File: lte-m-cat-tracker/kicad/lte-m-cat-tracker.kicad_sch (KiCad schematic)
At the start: 35 parts, among them J1 JST-PH-2mm-2P, J2 USB-C-16P, SW1 MSK12C02, U1 SIM7080G-M, U2 ESP32-C3, U3 LIS2DW12TR, U4 TP4056, U5 XC6220B331MR-G

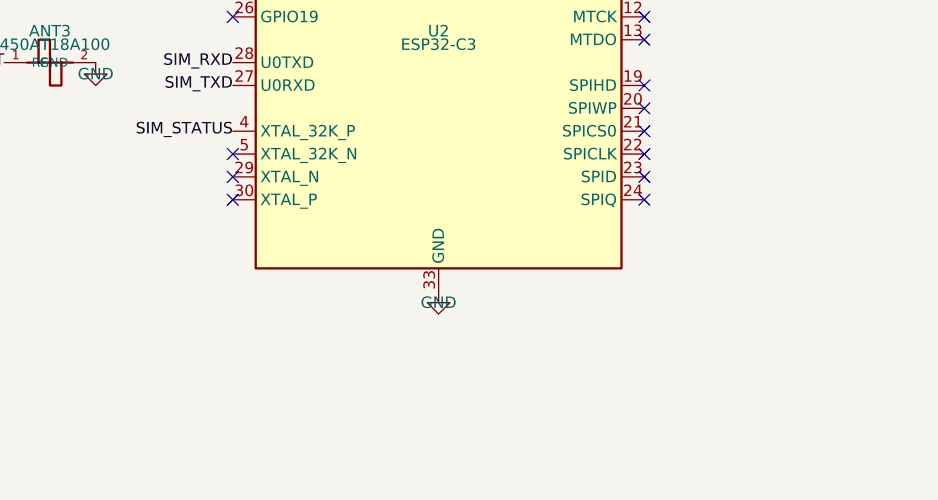
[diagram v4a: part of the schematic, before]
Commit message: 回路図に水晶Y1(C648974)+C16/C17を反映・schematic-parity解消（ネットリスト検証でPCBと一致確認・ERC水晶起因エラーなし）
Co-Authored-By: Claude Fable 5 <noreply@anthropic.com>
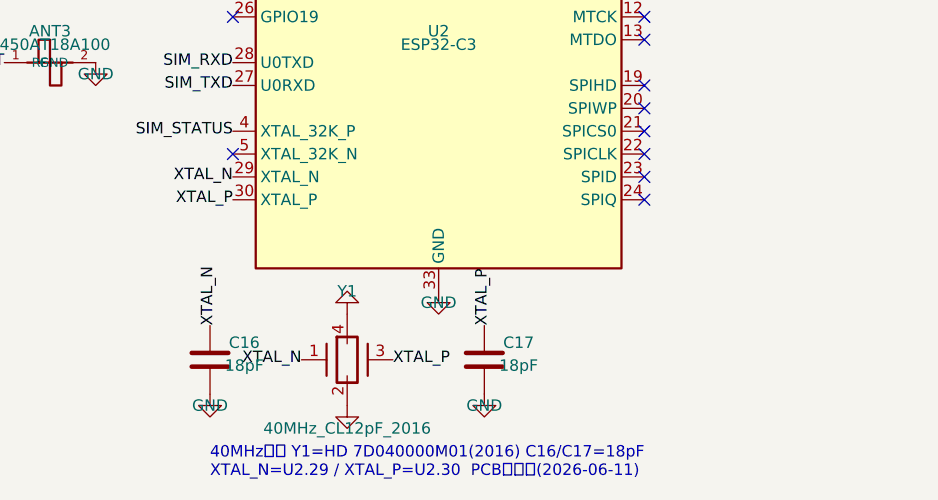
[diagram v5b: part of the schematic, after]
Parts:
- added C16, C17: 18pF, Capacitor_SMD:C_0402_1005Metric, symbol Device:C
- added Y1: 40MHz_CL12pF_2016, Crystal:Crystal_SMD_2016-4Pin_2.0x1.6mm, symbol Device:Crystal_GND24
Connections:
- net GND: now also C16.2, C17.2, Y1.2, Y1.4
- net XTAL_N: now reaches U2.29 (XTAL_N)
- net XTAL_N: now also C16.1, Y1.1
- net XTAL_P: now reaches U2.30 (XTAL_P)
- net XTAL_P: now also C17.1, Y1.3
- no-connect marks 27 -> 25
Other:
- note added: "40MHz水晶 Y1=HD 7D040000M01(2016) C16/C17=18pF XTAL_N=U2.29 / XTAL_P=U2.30 PCB実装済(2026-06-11)"
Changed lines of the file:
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@@
   (no_connect (at 111.76 215.9))
   (no_connect (at 66.04 210.82))
-  (no_connect (at 66.04 213.36))
-  (no_connect (at 66.04 215.9))
   (symbol (lib_id "Device:C") (at 63.49999999999999 165.1 0) (unit 1)
     (exclude_from_sim no)(in_bom yes)(on_board yes)
@@
     (property "Value" "GND"(at 93.98 81.28 0)(effects(font(size 1.27 1.27))))
     (property "Footprint" ""(at 93.98 80.01 0)(effects(font(size 1.27 1.27))hide)))
-)
+  (label "XTAL_N" (at 66.04 213.36 180)
+    (effects(font(size 1.27 1.27))(justify right))
+)
+  (label "XTAL_P" (at 66.04 215.9 180)
+    (effects(font(size 1.27 1.27))(justify right))
+)
+  (symbol (lib_id "Device:Crystal_GND24") (at 78.74 233.68 0) (unit 1)
+    (exclude_from_sim no)(in_bom yes)(on_board yes)
+    (property "Reference" "Y1" (at 78.74 226.06 0)(effects(font(size 1.27 1.27))))
+    (property "Value" "40MHz_CL12pF_2016" (at 78.74 241.3 0)(effects(font(size 1.27 1.27))))
+    (property "Footprint" "Crystal:Crystal_SMD_2016-4Pin_2.0x1.6mm" (at 78.74 233.68 0)(effects(font(size 1.27 1.27))hide))
+    (property "LCSC" "C648974" (at 78.74 233.68 0)(effects(font(size 1.27 1.27))hide))
+  )
+  (label "XTAL_N" (at 73.66 233.68 180)
+    (effects(font(size 1.27 1.27))(justify right))
+)
+  (label "XTAL_P" (at 83.82 233.68 0)
+    (effects(font(size 1.27 1.27))(justify left))
+)
+  (symbol (lib_id "power:GND") (at 78.74 238.76 0)(unit 1)
+    (exclude_from_sim no)(in_bom no)(on_board no)
+    (property "Reference" "#PWR"(at 78.74 241.3 0)(effects(font(size 1.27 1.27))hide))
+    (property "Value" "GND"(at 78.74 240.03 0)(effects(font(size 1.27 1.27))hide))
+    (property "Footprint" ""(at 78.74 238.76 0)(effects(font(size 1.27 1.27))hide)))
+  (symbol (lib_id "power:GND") (at 78.74 228.6 180)(unit 1)
+    (exclude_from_sim no)(in_bom no)(on_board no)
+    (property "Reference" "#PWR"(at 78.74 226.06 0)(effects(font(size 1.27 1.27))hide))
+    (property "Value" "GND"(at 78.74 227.33 0)(effects(font(size 1.27 1.27))hide))
+    (property "Footprint" ""(at 78.74 228.6 0)(effects(font(size 1.27 1.27))hide)))
+  (symbol (lib_id "Device:C") (at 63.5 233.68 0) (unit 1)
+    (exclude_from_sim no)(in_bom yes)(on_board yes)
+    (property "Reference" "C16" (at 67.31 231.775 0)(effects(font(size 1.27 1.27))))
+    (property "Value" "18pF" (at 67.31 234.315 0)(effects(font(size 1.27 1.27))))
+    (property "Footprint" "Capacitor_SMD:C_0402_1005Metric" (at 63.5 233.68 0)(effects(font(size 1.27 1.27))hide))
+    (property "LCSC" "C1555(発注前要確認)" (at 63.5 233.68 0)(effects(font(size 1.27 1.27))hide))
+  )
+  (label "XTAL_N" (at 63.5 229.87 270)
+    (effects(font(size 1.27 1.27))(justify left))
+)
+  (symbol (lib_id "power:GND") (at 63.5 237.49 0)(unit 1)
+    (exclude_from_sim no)(in_bom no)(on_board no)
+    (property "Reference" "#PWR"(at 63.5 240.03 0)(effects(font(size 1.27 1.27))hide))
+    (property "Value" "GND"(at 63.5 238.76 0)(effects(font(size 1.27 1.27))))
+    (property "Footprint" ""(at 63.5 237.49 0)(effects(font(size 1.27 1.27))hide)))
+  (symbol (lib_id "Device:C") (at 93.98 233.68 0) (unit 1)
+    (exclude_from_sim no)(in_bom yes)(on_board yes)
+    (property "Reference" "C17" (at 97.79 231.775 0)(effects(font(size 1.27 1.27))))
+    (property "Value" "18pF" (at 97.79 234.315 0)(effects(font(size 1.27 1.27))))
+    (property "Footprint" "Capacitor_SMD:C_0402_1005Metric" (at 93.98 233.68 0)(effects(font(size 1.27 1.27))hide))
+    (property "LCSC" "C1555(発注前要確認)" (at 93.98 233.68 0)(effects(font(size 1.27 1.27))hide))
+  )
+  (label "XTAL_P" (at 93.98 229.87 270)
+    (effects(font(size 1.27 1.27))(justify left))
+)
+  (symbol (lib_id "power:GND") (at 93.98 237.49 0)(unit 1)
+    (exclude_from_sim no)(in_bom no)(on_board no)
+    (property "Reference" "#PWR"(at 93.98 240.03 0)(effects(font(size 1.27 1.27))hide))
+    (property "Value" "GND"(at 93.98 238.76 0)(effects(font(size 1.27 1.27))))
+    (property "Footprint" ""(at 93.98 237.49 0)(effects(font(size 1.27 1.27))hide)))
+  (text "40MHz水晶 Y1=HD 7D040000M01(2016) C16/C17=18pF\nXTAL_N=U2.29 / XTAL_P=U2.30  PCB実装済(2026-06-11)"
+    (at 63.5 245.11 0)(effects(font(size 1.27 1.27))(justify left)))
+)

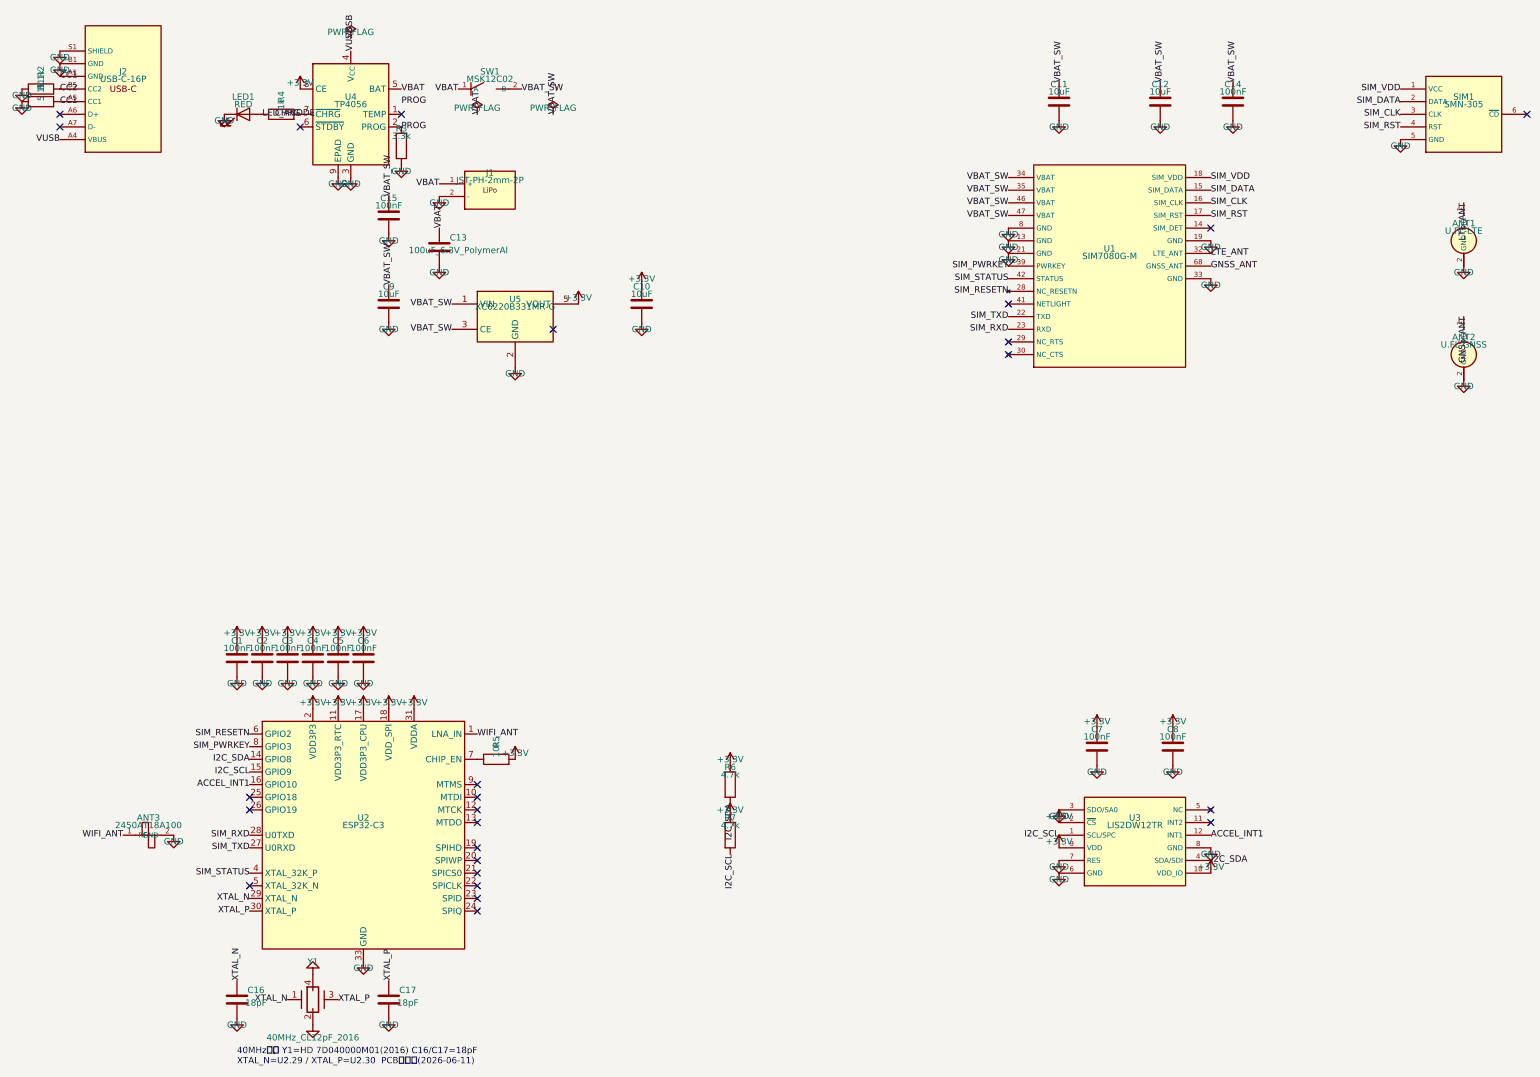
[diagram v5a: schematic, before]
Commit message: 回路図同期完了: UART1ピン修正・VDD_EXT/U6/C18/C19追加・netlist検証でPCBと一致
- U1シンボル TXD/RXD 22/23→1/2・pin46/47 NC化・VDD_EXTピン40新設
- SIM_RESETN消滅・U2側_33ネット化・U6(TXB0104)シンボル+パスコン2個
- フットプリント実体化(TXB0104_RGY14/C_0402)・ERC24件(増分は許容クラス)

Co-Authored-By: Claude Fable 5 <noreply@anthropic.com>
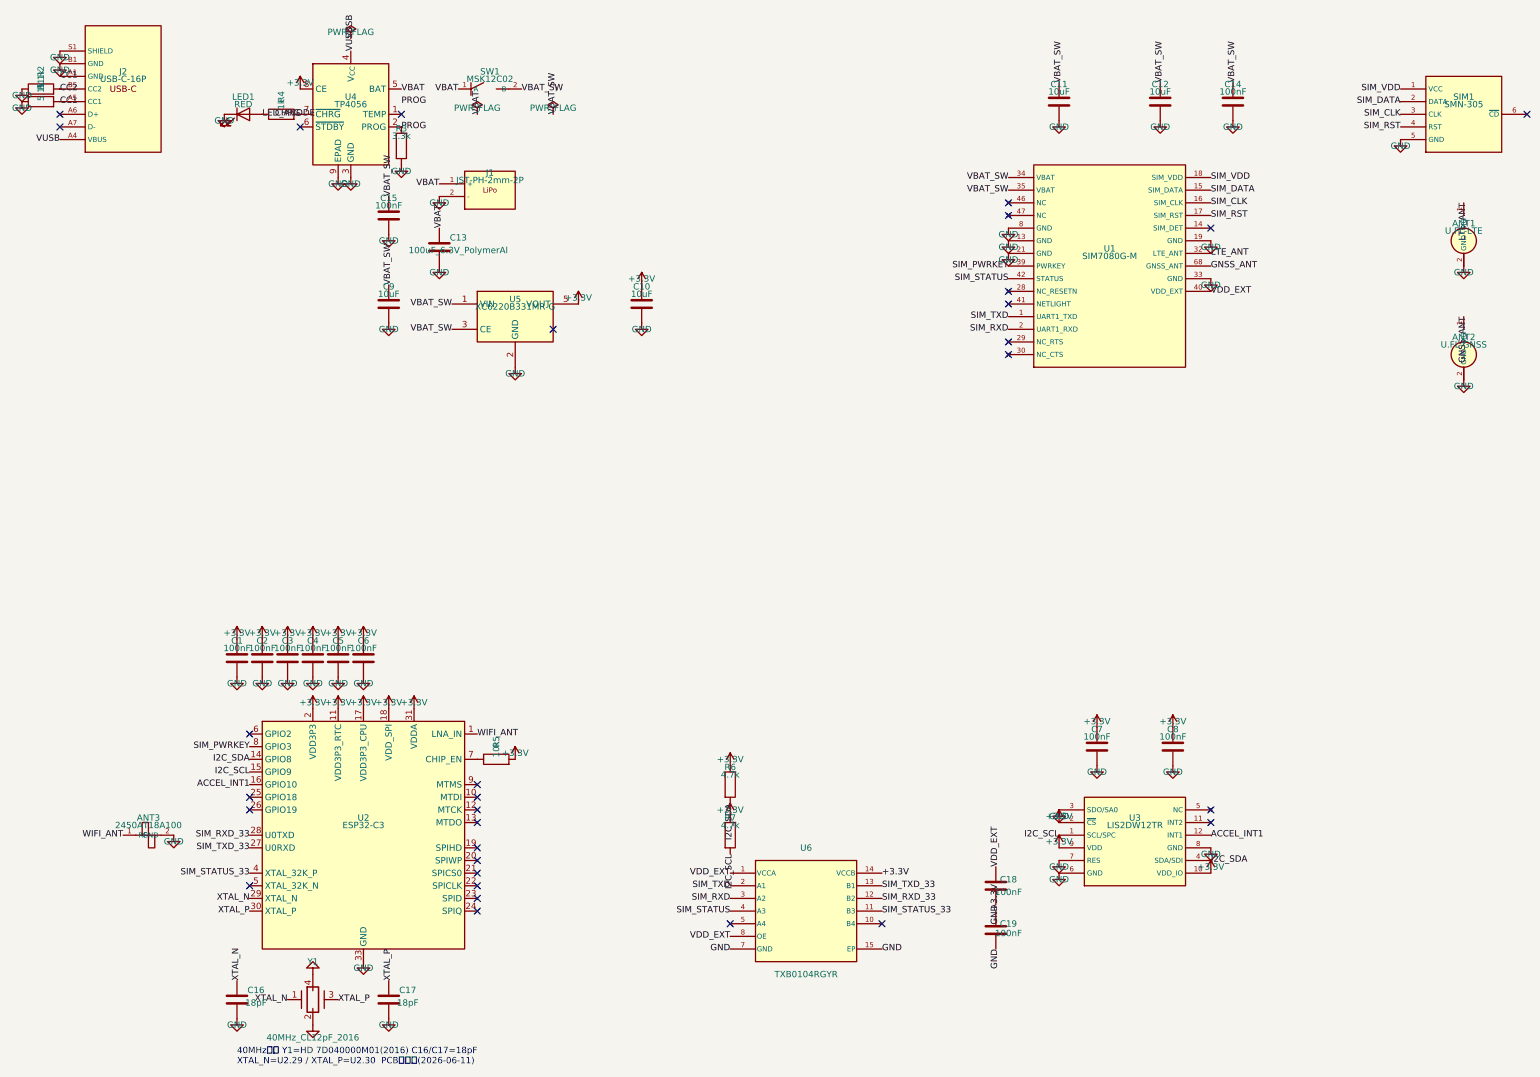
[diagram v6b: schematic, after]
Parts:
- added C18, C19: 100nF, lte-m-custom:C_0402, symbol Device:C
- added U6: TXB0104RGYR, lte-m-custom:TXB0104_RGY14, symbol Custom:TXB0104
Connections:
- net +3.3V: now also C19.1, U6.14 (VCCB)
- net GND: now also C18.2, C19.2, U6.15 (EP), U6.7 (GND)
- net SIM_RXD: now also U1.2 (UART1_RXD), U6.3 (A2); no longer U1.23 (RXD), U2.28 (U0TXD)
- net SIM_STATUS: now also U6.4 (A3); no longer U2.4 (XTAL_32K_P)
- net SIM_TXD: now also U1.1 (UART1_TXD), U6.2 (A1); no longer U1.22 (TXD), U2.27 (U0RXD)
- net VBAT_SW: no longer U1.46 (VBAT), U1.47 (VBAT)
- net SIM_RESETN: no longer names the net of U1.28 (NC_RESETN)
- net SIM_RESETN: no longer U2.6 (GPIO2)
- new net SIM_RXD_33: U2.28 (U0TXD), U6.12 (B2)
- new net SIM_STATUS_33: U2.4 (XTAL_32K_P), U6.11 (B3)
- new net SIM_TXD_33: U2.27 (U0RXD), U6.13 (B1)
- new net VDD_EXT: C18.1, U1.40 (VDD_EXT), U6.1 (VCCA), U6.8 (OE)
- no-connect marks 25 -> 31
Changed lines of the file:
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@@
     (effects(font(size 1.27 1.27))(justify right))
 )
-  (label "VBAT_SW" (at 218.44 73.66 180)
-    (effects(font(size 1.27 1.27))(justify right))
-)
-  (label "VBAT_SW" (at 218.44 76.2 180)
-    (effects(font(size 1.27 1.27))(justify right))
-)
+  (no_connect (at 218.44 73.66))
+  (no_connect (at 218.44 76.2))
   (symbol (lib_id "power:GND") (at 218.44 78.74 0)(unit 1)
     (exclude_from_sim no)(in_bom no)(on_board no)
@@
     (effects(font(size 1.27 1.27))(justify right))
 )
-  (label "SIM_RESETN" (at 218.44 91.44 180)
-    (effects(font(size 1.27 1.27))(justify right))
-)
+  (no_connect (at 218.44 91.44))
   (no_connect (at 218.44 93.98))
   (label "SIM_TXD" (at 218.44 96.52 180)
@@
   (no_connect (at 218.44 101.6))
   (no_connect (at 218.44 104.14))
+  (label "VDD_EXT" (at 259.08 91.44 0)
+    (effects(font(size 1.27 1.27))(justify left))
+)
   (label "SIM_VDD" (at 259.08 68.58 0)
     (effects(font(size 1.27 1.27))(justify left))
@@
     (effects(font(size 1.27 1.27))(justify left))
 )
-  (label "SIM_TXD" (at 66.04 203.2 180)
-    (effects(font(size 1.27 1.27))(justify right))
-)
-  (label "SIM_RXD" (at 66.04 200.66 180)
+  (label "SIM_TXD_33" (at 66.04 203.2 180)
+    (effects(font(size 1.27 1.27))(justify right))
+)
+  (label "SIM_RXD_33" (at 66.04 200.66 180)
     (effects(font(size 1.27 1.27))(justify right))
 )
@@
     (effects(font(size 1.27 1.27))(justify right))
 )
-  (label "SIM_RESETN" (at 66.04 180.34 180)
-    (effects(font(size 1.27 1.27))(justify right))
-)
-  (label "SIM_STATUS" (at 66.04 208.28 180)
+  (no_connect (at 66.04 180.34))
+  (label "SIM_STATUS_33" (at 66.04 208.28 180)
     (effects(font(size 1.27 1.27))(justify right))
 )
@@
   (text "40MHz水晶 Y1=HD 7D040000M01(2016) C16/C17=18pF\nXTAL_N=U2.29 / XTAL_P=U2.30  PCB実装済(2026-06-11)"
     (at 63.5 245.11 0)(effects(font(size 1.27 1.27))(justify left)))
-)
+  (symbol (lib_id "Custom:TXB0104") (at 177.8 215.9 0) (unit 1)
+    (exclude_from_sim no)(in_bom yes)(on_board yes)
+    (property "Reference" "U6" (at 177.8 203.20000000000002 0)(effects(font(size 1.27 1.27))))
+    (property "Value" "TXB0104RGYR" (at 177.8 228.6 0)(effects(font(size 1.27 1.27))))
+    (property "Footprint" "lte-m-custom:TXB0104_RGY14" (at 177.8 215.9 0)(effects(font(size 1.27 1.27))hide))
+    (property "LCSC" "C400708" (at 177.8 215.9 0)(effects(font(size 1.27 1.27))hide))
+  )
+  (label "VDD_EXT" (at 162.56 208.28 180)
+    (effects(font(size 1.27 1.27))(justify right))
+)
+  (label "SIM_TXD" (at 162.56 210.82 180)
+    (effects(font(size 1.27 1.27))(justify right))
+)
+  (label "SIM_RXD" (at 162.56 213.36 180)
+    (effects(font(size 1.27 1.27))(justify right))
+)
+  (label "SIM_STATUS" (at 162.56 215.9 180)
+    (effects(font(size 1.27 1.27))(justify right))
+)
+  (no_connect (at 162.56 218.44))
+  (label "VDD_EXT" (at 162.56 220.98000000000002 180)
+    (effects(font(size 1.27 1.27))(justify right))
+)
+  (label "GND" (at 162.56 223.52 180)
+    (effects(font(size 1.27 1.27))(justify right))
+)
+  (label "+3.3V" (at 193.04000000000002 208.28 0)
+    (effects(font(size 1.27 1.27))(justify left))
+)
+  (label "SIM_TXD_33" (at 193.04000000000002 210.82 0)
+    (effects(font(size 1.27 1.27))(justify left))
+)
+  (label "SIM_RXD_33" (at 193.04000000000002 213.36 0)
+    (effects(font(size 1.27 1.27))(justify left))
+)
+  (label "SIM_STATUS_33" (at 193.04000000000002 215.9 0)
+    (effects(font(size 1.27 1.27))(justify left))
+)
+  (no_connect (at 193.04000000000002 218.44))
+  (label "GND" (at 193.04000000000002 223.52 0)
+    (effects(font(size 1.27 1.27))(justify left))
+)
+  (symbol (lib_id "Device:C") (at 215.9 210.82 0) (unit 1)
+    (exclude_from_sim no)(in_bom yes)(on_board yes)
+    (property "Reference" "C18" (at 218.44 209.54999999999998 0)(effects(font(size 1.27 1.27))))
+    (property "Value" "100nF" (at 218.44 212.09 0)(effects(font(size 1.27 1.27))))
+    (property "Footprint" "lte-m-custom:C_0402" (at 215.9 210.82 0)(effects(font(size 1.27 1.27))hide))
+    (property "LCSC" "C14663" (at 215.9 210.82 0)(effects(font(size 1.27 1.27))hide))
+  )
+  (label "VDD_EXT" (at 215.9 207.01 90)
+    (effects(font(size 1.27 1.27))(justify left))
+)
+  (label "GND" (at 215.9 214.63 270)
+    (effects(font(size 1.27 1.27))(justify right))
+)
+  (symbol (lib_id "Device:C") (at 215.9 219.71 0) (unit 1)
+    (exclude_from_sim no)(in_bom yes)(on_board yes)
+    (property "Reference" "C19" (at 218.44 218.44 0)(effects(font(size 1.27 1.27))))
+    (property "Value" "100nF" (at 218.44 220.35000000000002 0)(effects(font(size 1.27 1.27))))
+    (property "Footprint" "lte-m-custom:C_0402" (at 215.9 219.08 0)(effects(font(size 1.27 1.27))hide))
+    (property "LCSC" "C14663" (at 215.9 219.08 0)(effects(font(size 1.27 1.27))hide))
+  )
+  (label "+3.3V" (at 215.9 215.9 90)
+    (effects(font(size 1.27 1.27))(justify left))
+)
+  (label "GND" (at 215.9 223.52 270)
+    (effects(font(size 1.27 1.27))(justify right))
+)
+)

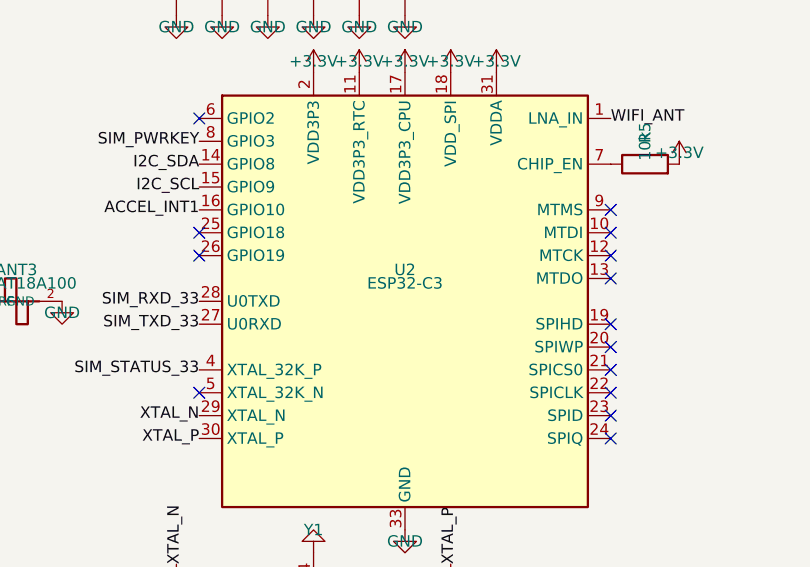
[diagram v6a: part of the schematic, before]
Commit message: 🔴 致命4件発見: フラッシュ非内蔵チップ選定(→FH4/C2858491へ変更済)・CHIP_EN未接続・GPIO2浮き・書き込み手段なし
- U2全パッドをEspressifデータシートFigure 2-1と照合
- C2838500(無印=Flash無)では実行不能だった→ESP32-C3FH4へBOM/回路図変更
- EN/GPIO2/USB書き込みの対策案をDESIGN.mdに明記(実装は次セッション)

Co-Authored-By: Claude Fable 5 <noreply@anthropic.com>
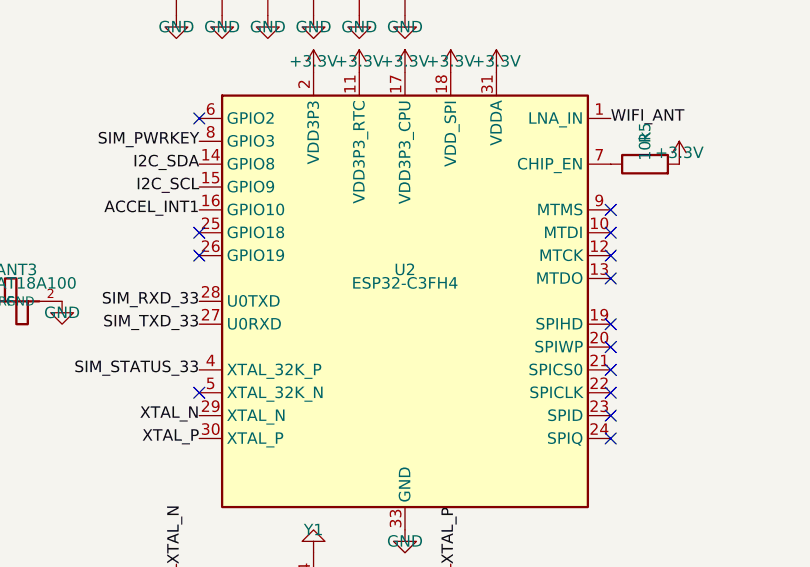
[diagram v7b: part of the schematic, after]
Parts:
- U2: value ESP32-C3 -> ESP32-C3FH4; LCSC C2838500 -> C2858491
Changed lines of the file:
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@@
     (exclude_from_sim no)(in_bom yes)(on_board yes)
     (property "Reference" "U2" (at 88.9 197.16 0)(effects(font(size 1.27 1.27))))
-    (property "Value" "ESP32-C3" (at 88.9 198.66 0)(effects(font(size 1.27 1.27))))
+    (property "Value" "ESP32-C3FH4" (at 88.9 198.66 0)(effects(font(size 1.27 1.27))))
     (property "Footprint" "Package_DFN_QFN:QFN-32-1EP_5x5mm_P0.5mm_EP3.7x3.7mm" (at 88.9 200.66 0)(effects(font(size 1.27 1.27))hide))
-    (property "LCSC" "C2838500" (at 88.9 200.66 0)(effects(font(size 1.27 1.27))hide))
+    (property "LCSC" "C2858491" (at 88.9 200.66 0)(effects(font(size 1.27 1.27))hide))
   )
   (symbol (lib_id "power:+3.3V") (at 78.74 175.26 0)(unit 1)
